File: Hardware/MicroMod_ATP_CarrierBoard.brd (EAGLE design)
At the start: 86.4 x 55.9 mm, 216 parts, among them J19 QWIIC_RIGHT_ANGLE, J2 JTAG, J20 QWIIC_RIGHT_ANGLE, J21 1X04_SMD_STRAIGHT_COMBO, J4 USB_A_SMT_FEMALE, J6 MICROMOD-2222-C, J8 1X04_SMD_STRAIGHT_COMBO, U5 AP7361C-33

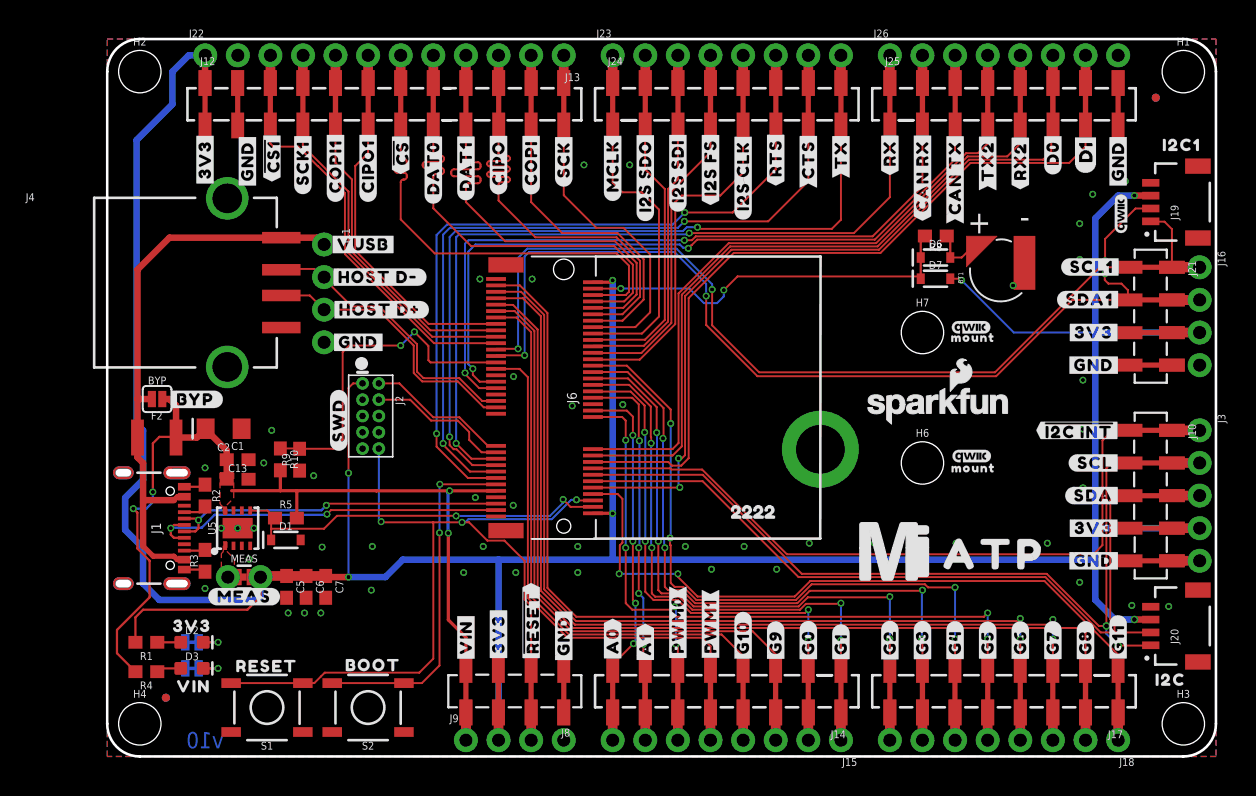
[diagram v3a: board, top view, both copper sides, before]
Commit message: Swaps out smaller qwiic labels for larger ones
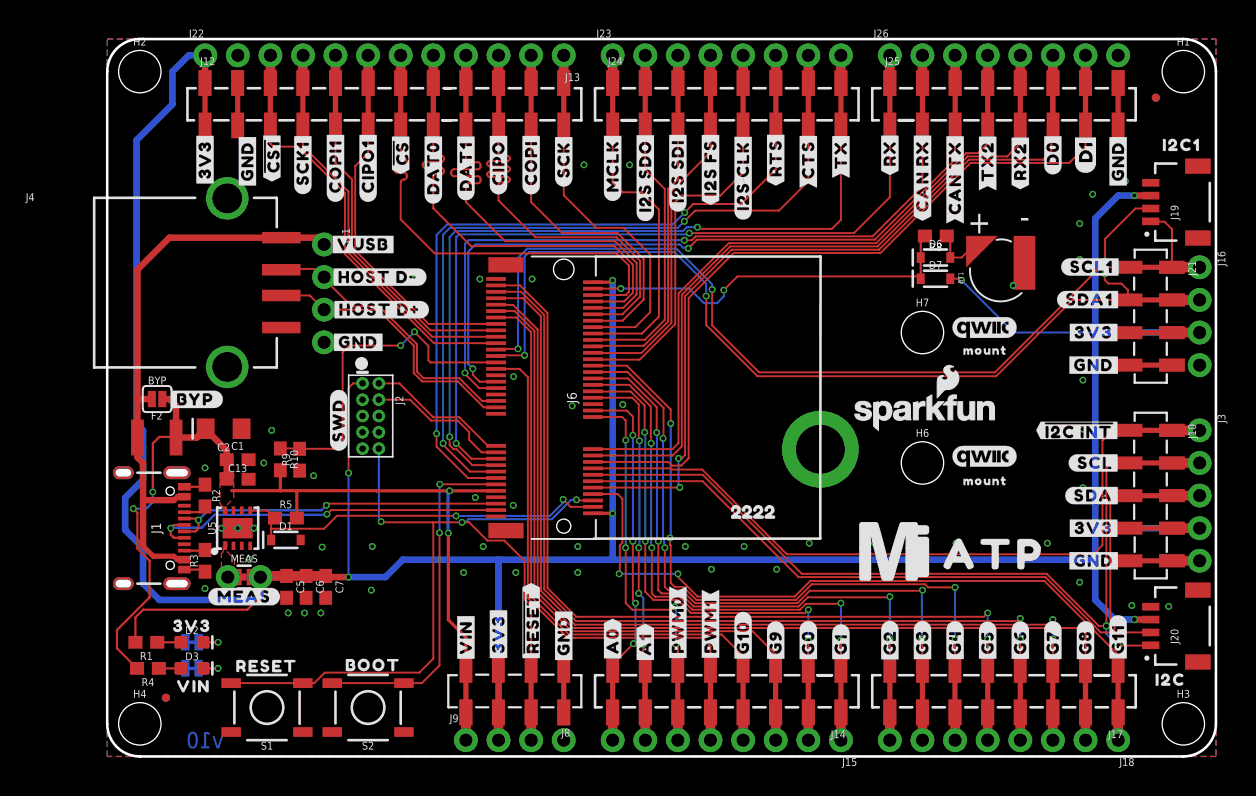
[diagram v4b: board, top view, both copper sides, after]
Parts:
- removed LOGO7: QWIIC_LOGO_3MM, SparkFun-Aesthetics:QWIIC_3MM
- LOGO2: value QWIIC_LOGO_3MM -> QWIIC_LOGO_5MM; device SparkFun-Aesthetics:QWIIC_3MM -> SparkFun-Aesthetics:QWIIC_5MM
- LOGO5, LOGO6, LOGO8: device SparkFun-Aesthetics:QWIIC_3MM -> SparkFun-Aesthetics:QWIIC_5MM
- moved LOGO2 21.7 mm to (68.3, 23.4), flipped to the bottom, turned to 0 degrees
- moved LOGO3 2.84 mm to (2.54, 6.35)
- moved U$143 1.40 mm to (68.3, 31.6)
- moved U$142 1.40 mm to (68.3, 21.5)
- moved U$139 1.38 mm to (68.4, 31.6)
- moved U$141 1.36 mm to (68.4, 21.5)
- moved LOGO1 1.14 mm to (63.8, 26.8)
- moved LOGO8 1.03 mm to (68.4, 33.4)
- moved LOGO5 1.03 mm to (68.3, 33.4)
- moved LOGO6 0.97 mm to (68.3, 23.4)
- moved R4 0.28 mm to (3.17, 6.86)
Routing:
- net GND: vias 48 -> 49
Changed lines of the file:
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@@
 <drawing>
 <settings>
-<setting alwaysvectorfont="no"/>
+<setting alwaysvectorfont="yes"/>
 <setting verticaltext="up"/>
 </settings>
-<grid distance="0.05" unitdist="inch" unit="inch" style="lines" multiple="1" display="yes" altdistance="0.005" altunitdist="inch" altunit="inch"/>
+<grid distance="0.01" unitdist="inch" unit="inch" style="lines" multiple="1" display="yes" altdistance="0.001" altunitdist="inch" altunit="inch"/>
 <layers>
 <layer number="1" name="Top" color="4" fill="1" visible="yes" active="yes"/>
@@
 <attribute name="VALUE" x="20.32" y="6.477" size="0.6096" layer="27" font="vector" ratio="20" rot="R180" align="top-center"/>
 </element>
-<element name="LOGO3" library="SparkFun-Aesthetics" package="OSHW-LOGO-MINI" value="OSHW-LOGOMINI" x="3.81" y="8.89" smashed="yes" rot="MR0"/>
+<element name="LOGO3" library="SparkFun-Aesthetics" package="OSHW-LOGO-MINI" value="OSHW-LOGOMINI" x="2.54" y="6.35" smashed="yes" rot="MR0"/>
 <element name="U$55" library="buzzard_labels (9)" package="22229" value="" x="47.625" y="19.05" smashed="yes"/>
 <element name="H5" library="SparkFun-Hardware" package="STAND-OFF-REFLOW-M2.5" value="STAND-OFF-REFLOW2.5MM_TALL" x="55.5498" y="23.9268" smashed="yes">
@@
 <attribute name="VALUE" x="3.048" y="9.652" size="0.6096" layer="27" font="vector" ratio="20" rot="R180" align="top-center"/>
 </element>
-<element name="R4" library="SparkFun-Resistors" package="0603" value="1k" x="3.048" y="6.604" smashed="yes" rot="R180">
-<attribute name="NAME" x="3.048" y="5.842" size="0.6096" layer="25" font="vector" ratio="20" rot="R180" align="bottom-center"/>
-<attribute name="PROD_ID" value="RES-07856" x="3.048" y="6.604" size="1.778" layer="27" rot="R180" display="off"/>
-<attribute name="VALUE" x="3.048" y="7.366" size="0.6096" layer="27" font="vector" ratio="20" rot="R180" align="top-center"/>
+<element name="R4" library="SparkFun-Resistors" package="0603" value="1k" x="3.175" y="6.858" smashed="yes" rot="R180">
+<attribute name="NAME" x="3.175" y="6.096" size="0.6096" layer="25" font="vector" ratio="20" rot="R180" align="bottom-center"/>
+<attribute name="PROD_ID" value="RES-07856" x="3.175" y="6.858" size="1.778" layer="27" rot="R180" display="off"/>
+<attribute name="VALUE" x="3.175" y="7.62" size="0.6096" layer="27" font="vector" ratio="20" rot="R180" align="top-center"/>
 </element>
 <element name="3V3_LED" library="SparkFun-Jumpers" package="SMT-JUMPER_2_NC_TRACE_SILK" package3d_urn="urn:adsk.eagle:package:39281/1" value="JUMPER-SMT_2_NC_TRACE_SILK" x="6.604" y="8.89" smashed="yes" rot="MR0">
@@
 <attribute name="VALUE" x="63.5" y="30.988" size="0.6096" layer="27" font="vector" ratio="20" align="top-center"/>
 </element>
-<element name="LOGO2" library="SparkFun-Aesthetics" package="QWIIC_3MM" value="QWIIC_LOGO_3MM" x="78.9686" y="42.2656" smashed="yes" rot="R90"/>
 <element name="U$62" library="headers_dup" package="ATP0" value="" x="69.088" y="15.748" smashed="yes"/>
 <element name="U$71" library="headers_dup" package="I2C4" value="" x="82.804" y="5.969" smashed="yes"/>
@@
 <element name="U$21" library="headtop" package="##I2C_INT##10" value="" x="75.692" y="25.4" smashed="yes"/>
 <element name="U$99" library="D1" package="D10" value="" x="76.2" y="45.339" smashed="yes" rot="R90"/>
-<element name="LOGO1" library="SparkFun-Aesthetics" package="SFE_LOGO_NAME_FLAME_.1" value="SFE_LOGO_NAME_FLAME.1_INCH" x="64.77" y="27.305" smashed="yes"/>
+<element name="LOGO1" library="SparkFun-Aesthetics" package="SFE_LOGO_NAME_FLAME_.1" value="SFE_LOGO_NAME_FLAME.1_INCH" x="63.754" y="26.797" smashed="yes"/>
 <element name="U$140" library="SparkFun-MicroMod" package="MICROMOD_MI_LOGO_1" value="" x="61.341" y="16.002" smashed="yes"/>
-<element name="U$139" library="headtop" package="MOUNT10" value="" x="67.437" y="32.639" smashed="yes"/>
-<element name="U$141" library="headtop" package="MOUNT10" value="" x="67.4624" y="22.479" smashed="yes"/>
-<element name="LOGO5" library="SparkFun-Aesthetics" package="QWIIC_3MM" value="QWIIC_LOGO_3MM" x="67.2846" y="33.4264" smashed="yes"/>
-<element name="LOGO6" library="SparkFun-Aesthetics" package="QWIIC_3MM" value="QWIIC_LOGO_3MM" x="67.3354" y="23.3934" smashed="yes"/>
-<element name="LOGO7" library="SparkFun-Aesthetics" package="QWIIC_3MM" value="QWIIC_LOGO_3MM" x="67.3354" y="23.3934" smashed="yes" rot="MR0"/>
-<element name="U$142" library="headtop" package="MOUNT10" value="" x="67.31" y="22.479" smashed="yes" rot="MR0"/>
-<element name="LOGO8" library="SparkFun-Aesthetics" package="QWIIC_3MM" value="QWIIC_LOGO_3MM" x="67.3354" y="33.4264" smashed="yes" rot="MR0"/>
-<element name="U$143" library="headtop" package="MOUNT10" value="" x="67.31" y="32.639" smashed="yes" rot="MR0"/>
+<element name="U$139" library="headtop" package="MOUNT10" value="" x="68.3854" y="31.639" smashed="yes"/>
+<element name="U$141" library="headtop" package="MOUNT10" value="" x="68.3854" y="21.479" smashed="yes"/>
+<element name="LOGO5" library="SparkFun-Aesthetics" package="QWIIC_5MM" value="QWIIC_LOGO_3MM" x="68.3098875" y="33.4264" smashed="yes"/>
+<element name="LOGO6" library="SparkFun-Aesthetics" package="QWIIC_5MM" value="QWIIC_LOGO_3MM" x="68.3098875" y="23.3934" smashed="yes"/>
+<element name="U$142" library="headtop" package="MOUNT10" value="" x="68.2854" y="21.479" smashed="yes" rot="MR0"/>
+<element name="LOGO8" library="SparkFun-Aesthetics" package="QWIIC_5MM" value="QWIIC_LOGO_3MM" x="68.3609125" y="33.4264" smashed="yes" rot="MR0"/>
+<element name="U$143" library="headtop" package="MOUNT10" value="" x="68.2854" y="31.639" smashed="yes" rot="MR0"/>
 <element name="U$144" library="SparkFun-MicroMod" package="MICROMOD_LOGO_1" value="" x="36.449" y="28.321" smashed="yes" rot="MR0"/>
 <element name="U$84" library="fl2" package="#CIPO#DAT0#6" value="" x="30.48" y="49.149" smashed="yes" rot="MR270"/>
 <element name="U$145" library="D1_again" package="D10" value="" x="76.2" y="54.356" smashed="yes" rot="MR270"/>
+<element name="LOGO2" library="SparkFun-Aesthetics" package="QWIIC_5MM" value="QWIIC_LOGO_5MM" x="68.326" y="23.368" smashed="yes" rot="MR0"/>
 </elements>
 <signals>
@@
 <wire x1="25.5143" y1="39.1795" x2="22.86" y2="41.8338" width="0.1524" layer="1"/>
 <wire x1="22.86" y1="52.07" x2="22.86" y2="54.61" width="0.762" layer="1"/>
-<wire x1="22.86" y1="41.8338" x2="22.86" y2="44.7318125" width="0.1524" layer="1"/>
+<wire x1="22.86" y1="44.7318125" x2="22.86" y2="41.8338" width="0.1524" layer="1"/>
 <wire x1="22.86" y1="44.7318125" x2="23.0632" y2="44.9350125" width="0.1524" layer="1" curve="-90"/>
 <wire x1="23.0632" y1="44.9350125" x2="23.12695" y2="44.9350125" width="0.1524" layer="1"/>
@@
 <contactref element="J8" pad="1"/>
 <wire x1="83.82" y1="15.24" x2="85.09" y2="15.24" width="0.762" layer="1"/>
+<via x="23.9522" y="37.1856" extent="1-16" drill="0.3048"/>
 </signal>
 <signal name="3.3V">
@@
 <wire x1="26.5684" y1="17.399" x2="26.543" y2="17.4244" width="0.254" layer="16"/>
 <wire x1="26.543" y1="20.563" x2="26.67" y2="20.69" width="0.254" layer="16"/>
-<wire x1="2.198" y1="6.604" x2="0.762" y2="8.04" width="0.1778" layer="1"/>
+<wire x1="2.325" y1="6.858" x2="0.762" y2="8.421" width="0.1778" layer="1"/>
 <via x="2.032" y="19.304" extent="1-16" drill="0.3048"/>
 <wire x1="2.3495" y1="18.9865" x2="2.032" y2="19.304" width="0.1778" layer="1"/>
@@
 <wire x1="3.556" y1="24.384" x2="4.064" y2="24.892" width="0.1778" layer="1"/>
 <wire x1="4.064" y1="24.892" x2="5.3608" y2="24.892" width="0.1778" layer="1"/>
-<wire x1="0.762" y1="8.04" x2="0.762" y2="9.8552" width="0.1778" layer="1"/>
+<wire x1="0.762" y1="8.421" x2="0.762" y2="9.8552" width="0.1778" layer="1"/>
 <wire x1="0.762" y1="9.8552" x2="3.302" y2="12.3952" width="0.1778" layer="1"/>
 <wire x1="3.302" y1="12.3952" x2="3.302" y2="15.24638125" width="0.1778" layer="1"/>
@@
 <wire x1="44.0436" y1="41.4274" x2="44.9834" y2="42.3672" width="0.1524" layer="16"/>
 <via x="44.9834" y="42.3672" extent="1-16" drill="0.3048"/>
-<wire x1="44.9834" y1="42.3672" x2="48.7172" y2="42.3672" width="0.1524" layer="1"/>
+<wire x1="49.3776" y1="43.0276" x2="45.6438" y2="43.0276" width="0.1524" layer="1"/>
+<wire x1="44.9834" y1="42.3672" x2="45.6438" y2="43.0276" width="0.1524" layer="1"/>
 <wire x1="26.4631875" y1="41.4274" x2="44.0436" y2="41.4274" width="0.1524" layer="16"/>
 <contactref element="J24" pad="6"/>
 <contactref element="J23" pad="6"/>
-<wire x1="48.7172" y1="42.3672" x2="52.07" y2="45.72" width="0.1524" layer="1"/>
+<wire x1="49.3776" y1="43.0276" x2="52.07" y2="45.72" width="0.1524" layer="1"/>
 <wire x1="52.07" y1="45.72" x2="52.07" y2="52.452" width="0.1524" layer="1"/>
 <wire x1="52.07" y1="52.452" x2="52.07" y2="54.61" width="0.762" layer="1"/>
@@
 <wire x1="44.452925" y1="41.1734" x2="44.958" y2="41.678475" width="0.1524" layer="16"/>
 <via x="44.958" y="41.678475" extent="1-16" drill="0.3048"/>
-<wire x1="44.958" y1="41.678475" x2="51.482875" y2="41.678475" width="0.1524" layer="1"/>
+<wire x1="52.321075" y1="42.516675" x2="45.7962" y2="42.516675" width="0.1524" layer="1"/>
+<wire x1="44.958" y1="41.678475" x2="45.7962" y2="42.516675" width="0.1524" layer="1"/>
 <wire x1="26.162" y1="40.64" x2="26.6954" y2="41.1734" width="0.1524" layer="16"/>
 <wire x1="26.6954" y1="41.1734" x2="44.452925" y2="41.1734" width="0.1524" layer="16"/>
 <contactref element="J24" pad="7"/>
-<wire x1="51.482875" y1="41.678475" x2="54.61" y2="44.8056" width="0.1524" layer="1"/>
+<wire x1="52.321075" y1="42.516675" x2="54.61" y2="44.8056" width="0.1524" layer="1"/>
 <contactref element="J23" pad="7"/>
 <wire x1="54.61" y1="52.07" x2="54.61" y2="54.61" width="0.762" layer="1"/>
@@
 <contactref element="R4" pad="1"/>
 <contactref element="D3" pad="A"/>
-<wire x1="3.898" y1="6.604" x2="4.152" y2="6.858" width="0.1778" layer="1"/>
-<wire x1="4.152" y1="6.858" x2="5.727" y2="6.858" width="0.1778" layer="1"/>
+<wire x1="4.025" y1="6.858" x2="5.727" y2="6.858" width="0.1778" layer="1"/>
 </signal>
 <signal name="N$3">

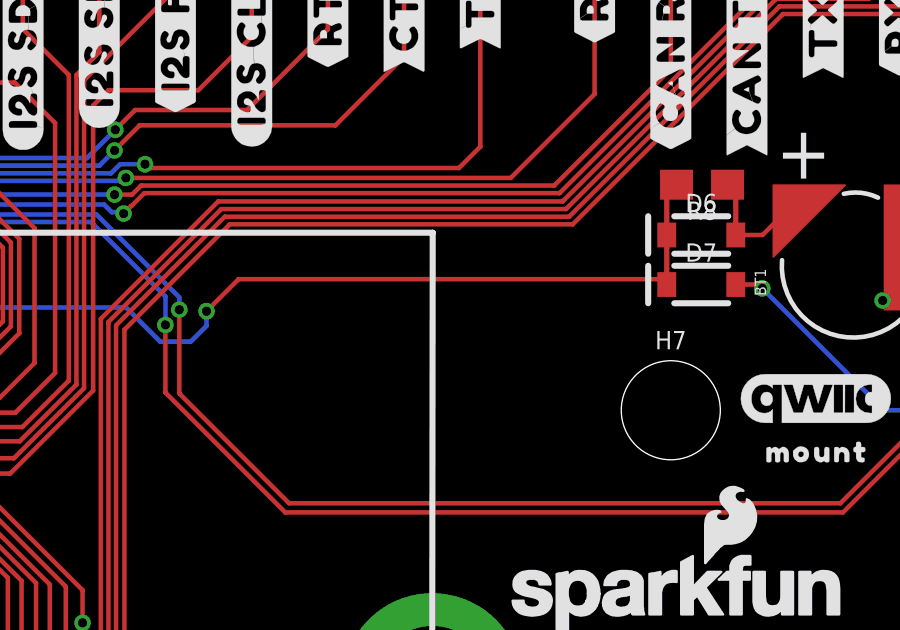
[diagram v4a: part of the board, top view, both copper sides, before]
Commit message: Adds testpoint for the RTC lines, adds text for VIN range and warning about using USB host and USB-C at the same time
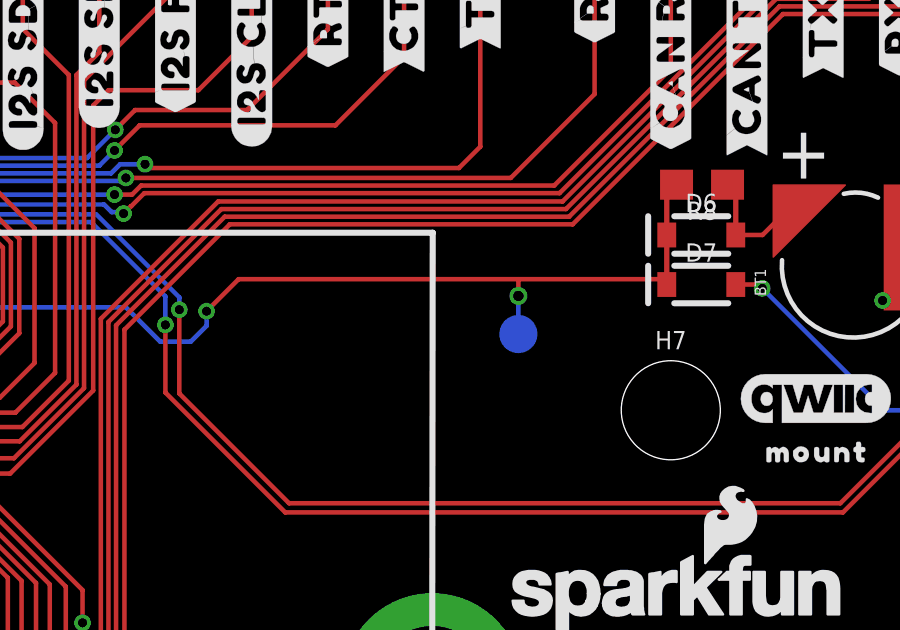
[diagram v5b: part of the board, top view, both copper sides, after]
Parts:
- added TP1: TEST-POINT3X5, SparkFun-Connectors:PAD.03X.05
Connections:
- net RTC_3V: now also TP1.P$1
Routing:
- net RTC_3V: track 30.7 -> 32.6 mm, vias 2 -> 3
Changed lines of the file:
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@@
 <drawing>
 <settings>
-<setting alwaysvectorfont="yes"/>
+<setting alwaysvectorfont="no"/>
 <setting verticaltext="up"/>
 </settings>
-<grid distance="0.01" unitdist="inch" unit="inch" style="lines" multiple="1" display="yes" altdistance="0.001" altunitdist="inch" altunit="inch"/>
+<grid distance="0.05" unitdist="inch" unit="inch" style="lines" multiple="1" display="yes" altdistance="0.005" altunitdist="inch" altunit="inch"/>
 <layers>
 <layer number="1" name="Top" color="4" fill="1" visible="yes" active="yes"/>
@@
 <element name="U$145" library="D1_again" package="D10" value="" x="76.2" y="54.356" smashed="yes" rot="MR270"/>
 <element name="LOGO2" library="SparkFun-Aesthetics" package="QWIIC_5MM" value="QWIIC_LOGO_5MM" x="68.326" y="23.368" smashed="yes" rot="MR0"/>
+<element name="TP1" library="SparkFun-Connectors" package="PAD.03X.05" value="TEST-POINT3X5" x="58.42" y="35.56" smashed="yes" rot="MR0"/>
 </elements>
 <signals>
@@
 <wire x1="63.1882" y1="37.3888" x2="63.366" y2="37.211" width="0.1524" layer="1"/>
 <wire x1="48.02555" y1="36.322" x2="49.09235" y2="37.3888" width="0.1524" layer="1"/>
-<wire x1="63.1882" y1="37.3888" x2="49.09235" y2="37.3888" width="0.1524" layer="1"/>
+<wire x1="63.1882" y1="37.3888" x2="58.42" y2="37.3888" width="0.1524" layer="1"/>
+<wire x1="49.09235" y1="37.3888" x2="58.42" y2="37.3888" width="0.1524" layer="1"/>
 <wire x1="63.366" y1="38.862" x2="63.366" y2="40.0878" width="0.1778" layer="1"/>
 <wire x1="63.366" y1="40.0878" x2="63.754" y2="40.4758" width="0.1778" layer="1"/>
+<contactref element="TP1" pad="P$1"/>
+<wire x1="58.42" y1="37.3888" x2="58.42" y2="36.83" width="0.1524" layer="1"/>
+<via x="58.42" y="36.83" extent="1-16" drill="0.35"/>
+<wire x1="58.42" y1="36.83" x2="58.42" y2="35.56" width="0.1524" layer="16"/>
 </signal>
 <signal name="SWDIO">
